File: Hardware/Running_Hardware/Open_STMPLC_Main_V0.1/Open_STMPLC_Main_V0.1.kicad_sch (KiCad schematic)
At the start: 44 parts, among them J1 Screw_Terminal_01x02, J2 Simcard_Nano, J4 DE9_Pins, J5 TF-102, Q1 Q_PMOS, U1 LAN8720A, U4 ADM2587E, U5 W25Q64JVSSIQ, U6 TPD4E1U06DCKR, U7 TPS26600PWP, U8 UCC23513

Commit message: schematic updates v0.1
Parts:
- removed C11: 33pF, Capacitor_SMD:C_0603_1608Metric_Pad1.08x0.95mm_HandSolder, symbol Device:C_Small
- removed D2: ESDA5V3SC5, Package_TO_SOT_SMD:SOT-23-5, symbol Power_Protection:ESDA5V3SC5
- removed D4: SS34, symbol Device:D_Schottky_Small
- removed J2: Simcard_Nano, SimCard:TE_2336582-1, symbol Simcard_Holder_Nano:47553-2001
- removed Q1: Q_PMOS, symbol Device:Q_PMOS
- added D2, D6, D7: SS54, symbol Device:D_Schottky_Small
- added D4: BZT52C12, symbol Device:D_Zener_Small
- added D5: SMAJ33CA, Diode_SMD:D_SMA, symbol Diode:SMAJ33CA
- added J2: Screw_Terminal_01x02, symbol Connector:Screw_Terminal_01x02
- added Q1: SUD50P06, Package_TO_SOT_SMD:TO-252-3_TabPin2, symbol Transistor_FET:Q_PMOS_GDS
- added Q2: AO3400A, Package_TO_SOT_SMD:SOT-23, symbol Transistor_FET:AO3400A
- added R10: 1K, symbol Device:R_Small
- added R11: 470R, symbol Device:R_Small
- added R12, R13: 150R, Resistor_SMD:R_0603_1608Metric_Pad0.98x0.95mm_HandSolder, symbol Device:R_Small
- added R14: 10K, symbol Device:R_Small
- added R15: 100K, symbol Device:R_Small
- added R16, R27, R3: 10K, Resistor_SMD:R_0603_1608Metric_Pad0.98x0.95mm_HandSolder, symbol Device:R_Small
- added R17, R19, R20: 4.7K, Resistor_SMD:R_0603_1608Metric_Pad0.98x0.95mm_HandSolder, symbol Device:R_Small
- added R18: 15K, symbol Device:R_Small
- added R4: 1K, Resistor_SMD:R_0603_1608Metric_Pad0.98x0.95mm_HandSolder, symbol Device:R_Small
- added R5: 715K, Resistor_SMD:R_0603_1608Metric_Pad0.98x0.95mm_HandSolder, symbol Device:R_Small
- added R8: 11.8K, Resistor_SMD:R_0603_1608Metric_Pad0.98x0.95mm_HandSolder, symbol Device:R_Small
- added R9: 33.2K, Resistor_SMD:R_0603_1608Metric_Pad0.98x0.95mm_HandSolder, symbol Device:R_Small
- added U10: MAX31865xTP, Package_DFN_QFN:TQFN-20-1EP_5x5mm_P0.65mm_EP3.25x3.25mm, symbol Sensor_Temperature:MAX31865xTP
- added U11: MAX31856, Package_SO:TSSOP-14_4.4x5mm_P0.65mm, symbol Sensor_Temperature:MAX31856
- added U12: 6N137, Package_DIP:DIP-8_W7.62mm, symbol Isolator:6N137
- added U3: TPS1H200A, Package_SO:HVSSOP-8-1EP_3x3mm_P0.65mm_EP1.57x1.89mm_ThermalVias, symbol TPS1H200A:TPS1H200A
- added U9: TPS3430WDRC, Package_SON:VSON-10-1EP_3x3mm_P0.5mm_EP1.65x2.4mm, symbol Power_Supervisor:TPS3430WDRC
- C10: value 33pF -> 620nF; footprint Capacitor_SMD:C_0603_1608Metric_Pad1.08x0.95mm_HandSolder -> (none); JLCPCB_Part C107047 -> (none)
- C8: value 100nF -> 1uF; footprint Capacitor_SMD:C_0402_1005Metric_Pad0.74x0.62mm_HandSolder -> (none); JLCPCB_Part C77020 -> (none)
- C9: value 33pF -> 2.2uF; footprint Capacitor_SMD:C_0603_1608Metric_Pad1.08x0.95mm_HandSolder -> (none); JLCPCB_Part C107047 -> (none)
- D1: value SS34 -> SS54
- R2: value 10K -> 47R
- R6: value 10K -> 20K; JLCPCB_Part C25804 -> (none)
- R7: value 51K -> 30.1K; JLCPCB_Part C23196 -> (none)
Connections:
- net USIM_CLK is gone; now on net GND: C10.2
- net USIM_DATA is gone; now on an unnamed net: R6.1
- net USIM_DET is gone; now on an unnamed net: R7.1
- net USIM_RST is gone; now on an unnamed net: C9.2
- net +24V: now also C8.1, D2.1 (K), D7.2 (A), R5.2
- net +3V3: now also R16.2, R27.2, R3.2, U12.8 (VCC); no longer R7.2
- net GND: now also C8.2, U1.25 (VSS), D5.2 (A2), J2.2 (Pin_2), Q2.2 (S), R10.1, R14.1, U10.10 (GND), U10.16 (GND), U10.21 (GND), U11.14 (DGND), U12.5 (GND), U3.6 (GND), U3.9 (EP), U9.11 (GND), U9.5 (GND); no longer C10.1, C8.1, C9.1
- net at D1.1 (K), D3.1 (A1), J1.1 (Pin_1): now also D2.2 (A)
- net at C1.1, C2.1, R2.2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: now also D4.1 (K), Q1.3 (S)
- net at D1.2 (A): now also Q1.2 (D)
- net at R1.2, R2.1: now also D4.2 (A), Q1.1 (G)
- net IMON: now reaches U7.10 (IMON)
- net IMON: now also R9.2
- net at U7.11 (ILIM): now also R8.2
- net at U7.12 (dVdT): now also C9.1
- net at U7.14 (~{FLT}): now also R3.1, R4.2
- net at U7.17 (RTN), U7.8 (RTN): now also U7.6 (MODE), R8.1, R9.1
- net at U7.3 (UVLO): now also R6.2, R5.1
- net at U7.5 (OVP): now also R7.2
- net ~{SHDN}: now reaches U7.7 (~{SHDN})
- net at U8.1 (ANODE): now also R12.2
- net at U8.3 (CATHODE): now also R13.2
- removed net USIM_VDD: C8.2, R6.2
- new net: Q2.3 (D), R13.1
- new net: Q2.1 (G), R11.2, R14.2
- new net: R10.2, U3.4 (CL)
- new net: C10.1, R15.1, U3.5 (DELAY)
- new net: D7.1 (K), R15.2, R18.2, U3.8 (VS)
- new net: D5.1 (A1), D6.1 (K), J2.1 (Pin_1)
- new net: D6.2 (A), R18.1, U3.7 (OUT)
- new net: R16.1, R17.2, U3.3 (~{FAULT})
- new net: R19.2, U3.1 (IN)
- new net: R20.2, U3.2 (DIAG_EN)
- new net +5V: R12.1
- new net DIAG_OUT1: R20.1
- new net HS_OUT_1: R11.1
- new net IN_1: R27.1, U12.6 (VO)
- new net LS_OUT1: R19.1
- new net ~{FAULT}: R17.1, R4.1
- no-connect marks 6 -> 8
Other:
- note removed: "Sim card"
- moved on the sheet: C1, C2, D1, D3, J1, R1, R2, U7, U8

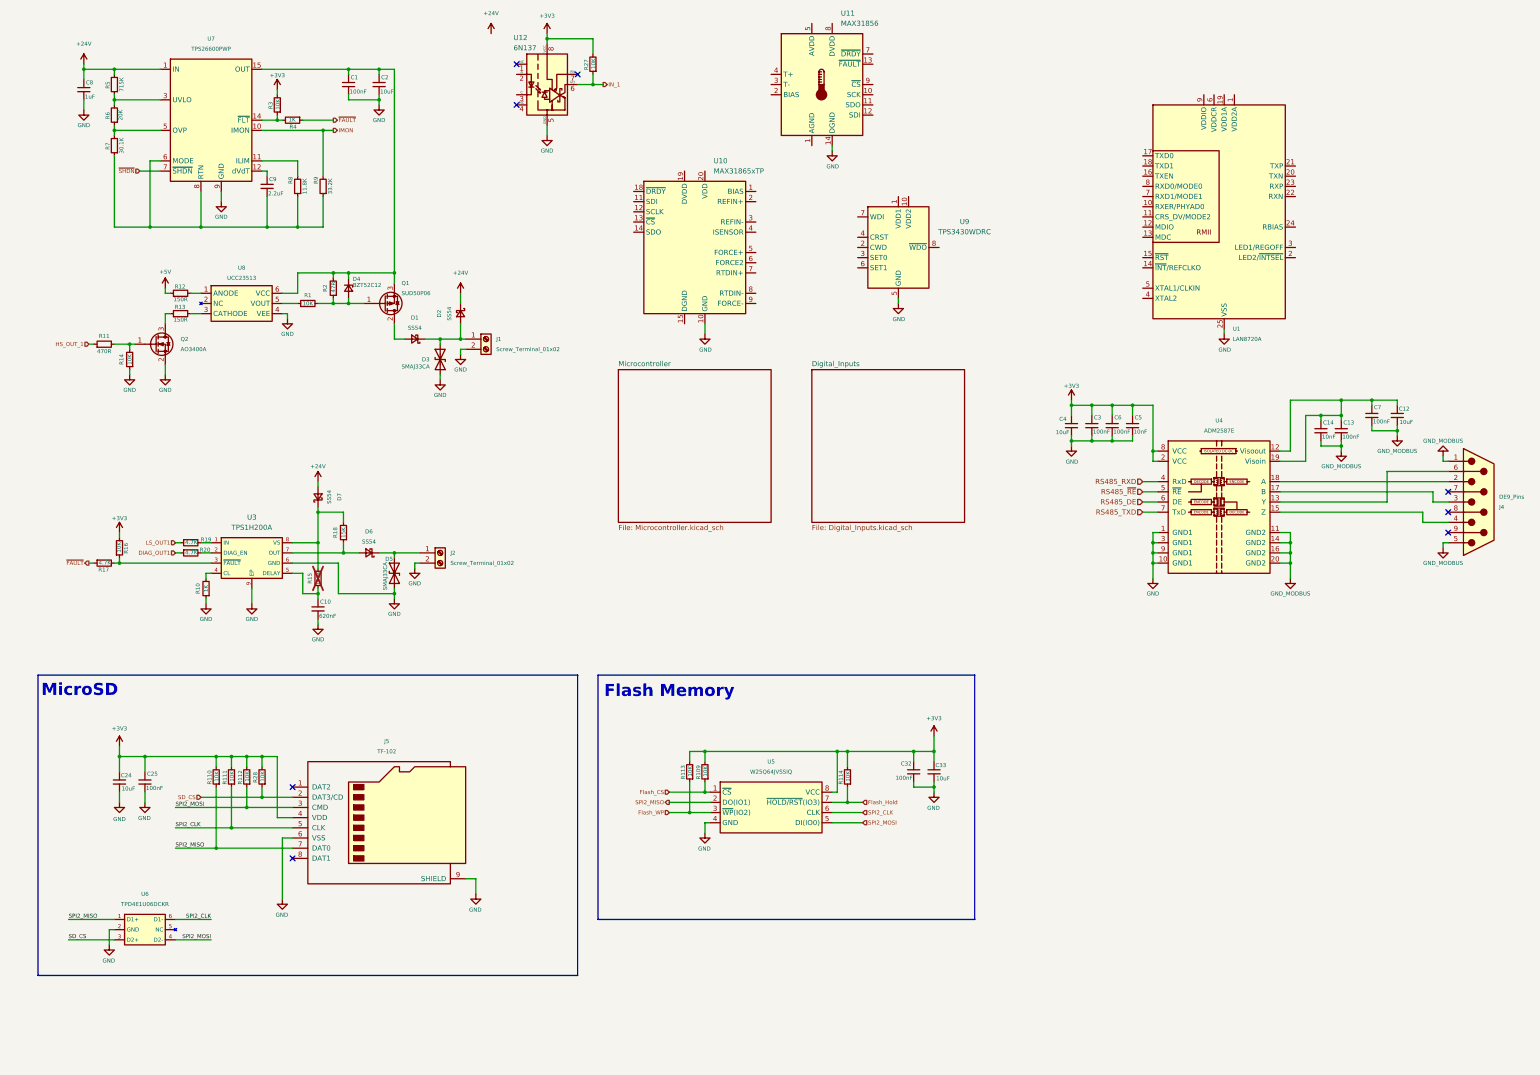
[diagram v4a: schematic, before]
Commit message: IO board schematic
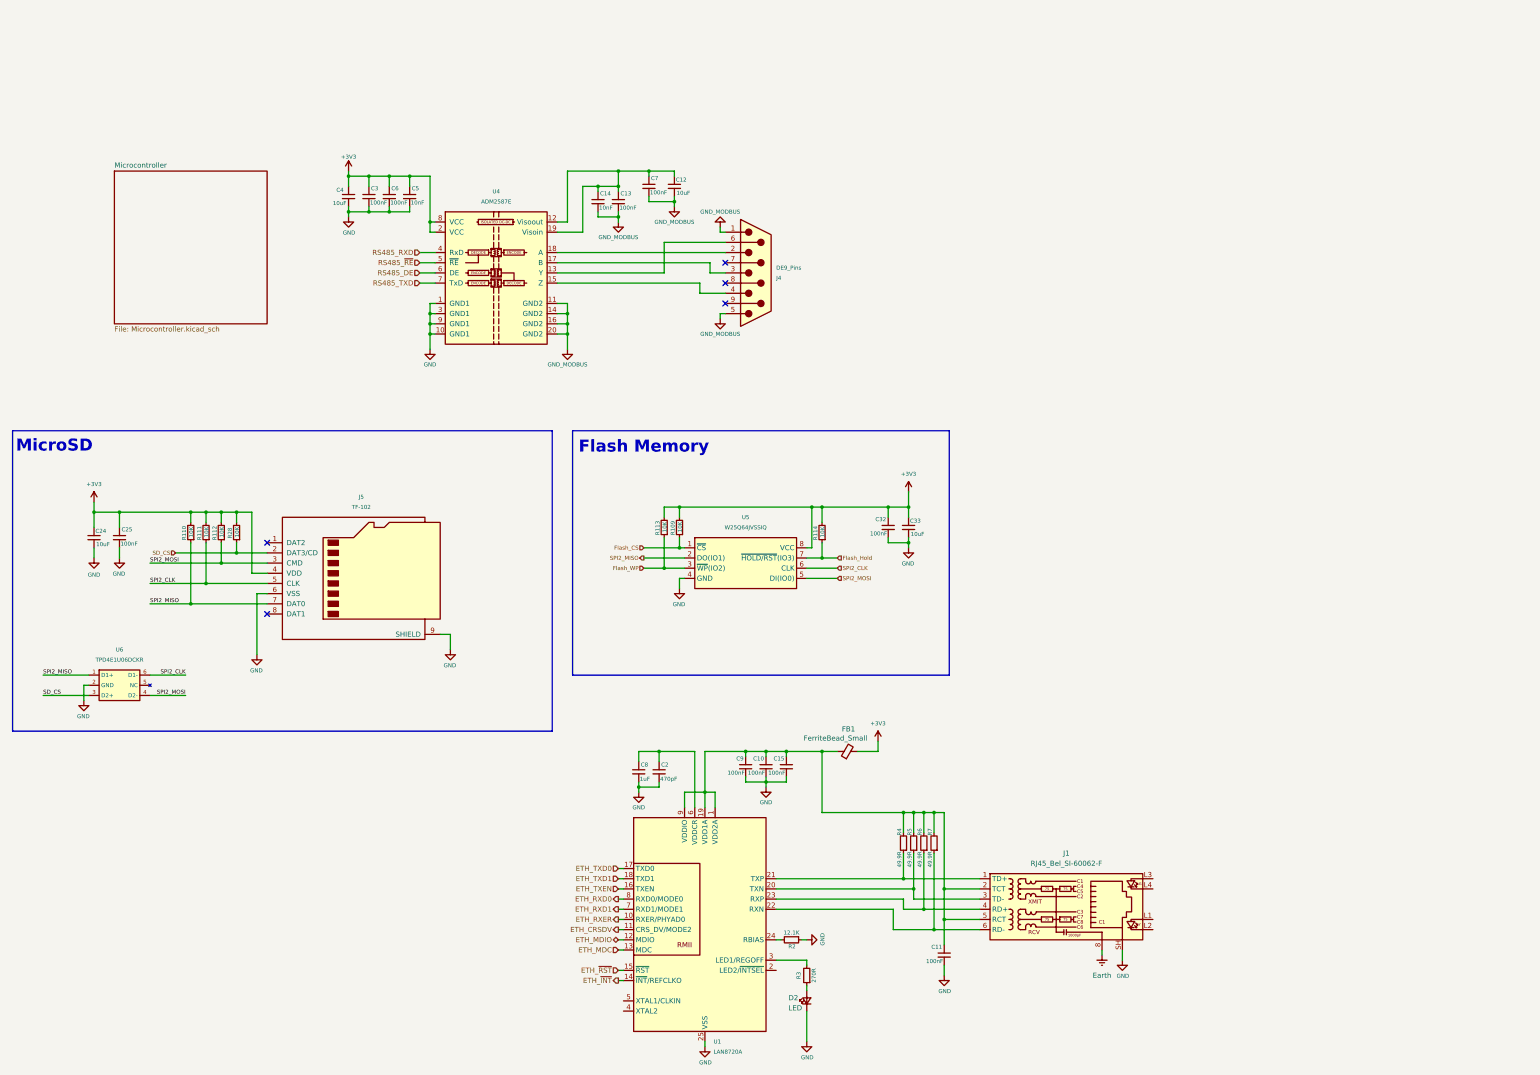
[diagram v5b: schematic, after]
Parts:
- removed C1: 100nF, symbol Device:C_Small
- removed D1, D2, D6, D7: SS54, symbol Device:D_Schottky_Small
- removed D3, D5: SMAJ33CA, Diode_SMD:D_SMA, symbol Diode:SMAJ33CA
- removed D4: BZT52C12, symbol Device:D_Zener_Small
- removed J1, J2: Screw_Terminal_01x02, symbol Connector:Screw_Terminal_01x02
- removed Q1: SUD50P06, Package_TO_SOT_SMD:TO-252-3_TabPin2, symbol Transistor_FET:Q_PMOS_GDS
- removed Q2: AO3400A, Package_TO_SOT_SMD:SOT-23, symbol Transistor_FET:AO3400A
- removed R1, R14: 10K, symbol Device:R_Small
- removed R10: 1K, symbol Device:R_Small
- removed R11: 470R, symbol Device:R_Small
- removed R12, R13: 150R, Resistor_SMD:R_0603_1608Metric_Pad0.98x0.95mm_HandSolder, symbol Device:R_Small
- removed R15: 100K, symbol Device:R_Small
- removed R16, R27: 10K, Resistor_SMD:R_0603_1608Metric_Pad0.98x0.95mm_HandSolder, symbol Device:R_Small
- removed R17, R19, R20: 4.7K, Resistor_SMD:R_0603_1608Metric_Pad0.98x0.95mm_HandSolder, symbol Device:R_Small
- removed R18: 15K, symbol Device:R_Small
- removed R8: 11.8K, Resistor_SMD:R_0603_1608Metric_Pad0.98x0.95mm_HandSolder, symbol Device:R_Small
- removed R9: 33.2K, Resistor_SMD:R_0603_1608Metric_Pad0.98x0.95mm_HandSolder, symbol Device:R_Small
- removed U10: MAX31865xTP, Package_DFN_QFN:TQFN-20-1EP_5x5mm_P0.65mm_EP3.25x3.25mm, symbol Sensor_Temperature:MAX31865xTP
- removed U11: MAX31856, Package_SO:TSSOP-14_4.4x5mm_P0.65mm, symbol Sensor_Temperature:MAX31856
- removed U12: 6N137, Package_DIP:DIP-8_W7.62mm, symbol Isolator:6N137
- removed U3: TPS1H200A, Package_SO:HVSSOP-8-1EP_3x3mm_P0.65mm_EP1.57x1.89mm_ThermalVias, symbol TPS1H200A:TPS1H200A
- removed U7: TPS26600PWP, Package_SO:HTSSOP-16-1EP_4.4x5mm_P0.65mm_EP3.4x5mm_Mask2.66x2.46mm_ThermalVias, symbol Power_Management:TPS26600PWP
- removed U8: UCC23513, Package_SO:SSO-6_6.8x4.6mm_P1.27mm_Clearance8mm, symbol UCC23153:UCC23513
- removed U9: TPS3430WDRC, Package_SON:VSON-10-1EP_3x3mm_P0.5mm_EP1.65x2.4mm, symbol Power_Supervisor:TPS3430WDRC
- added C11, C15: 100nF, Capacitor_SMD:C_0603_1608Metric_Pad1.08x0.95mm_HandSolder, symbol Device:C_Small
- added D2: LED, symbol Device:LED_Small
- added FB1: FerriteBead_Small, symbol Device:FerriteBead_Small
- added J1: RJ45_Bel_SI-60062-F, Connector_RJ:RJ45_Bel_SI-60062-F, symbol Connector:RJ45_Bel_SI-60062-F
- C10: value 620nF -> 100nF; footprint (none) -> Capacitor_SMD:C_0603_1608Metric_Pad1.08x0.95mm_HandSolder
- C2: value 10uF -> 470pF
- C9: value 2.2uF -> 100nF; footprint (none) -> Capacitor_SMD:C_0603_1608Metric_Pad1.08x0.95mm_HandSolder
- R2: value 47R -> 12.1K; footprint (none) -> Resistor_SMD:R_0603_1608Metric_Pad0.98x0.95mm_HandSolder
- R3: value 10K -> 270R; footprint Resistor_SMD:R_0603_1608Metric_Pad0.98x0.95mm_HandSolder -> (none)
- R4: value 1K -> 49.9R
- R5: value 715K -> 49.9R
- R6: value 20K -> 49.9R
- R7: value 30.1K -> 49.9R
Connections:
- net ~{FAULT} is gone; now on an unnamed net: R4.1
- net +3V3: now also FB1.2; no longer R3.2
- net GND: now also C9.2, R2.1, C11.2, C15.2, D2.1 (K), J1.SH
- net at R3.1: now also D2.2 (A); no longer R4.2
- net at R7.1: now also U1.22 (RXN), J1.6 (RD-); no longer C9.2
- net at R7.2: now also C10.1, C9.1, R4.2, R5.2, R6.2, U1.1 (VDD2A), U1.19 (VDD1A), U1.9 (VDDIO), C11.1, C15.1, FB1.1, J1.2 (TCT), J1.5 (RCT); no longer R6.1
- net at C2.1: now also C8.1, U1.6 (VDDCR); no longer R2.2
- net at R5.1: now also U1.20 (TXN), J1.3 (TD-); no longer R6.2
- net ETH_RXER: now reaches U1.10 (RXER/PHYAD0)
- net ETH_CRSDV: now reaches U1.11 (CRS_DV/MODE2)
- net ETH_MDIO: now reaches U1.12 (MDIO)
- net ETH_MDC: now reaches U1.13 (MDC)
- net ETH_~{INT}: now reaches U1.14 (~{INT}/REFCLKO)
- net ETH_~{RST}: now reaches U1.15 (~{RST})
- net ETH_TXEN: now reaches U1.16 (TXEN)
- net ETH_TXD0: now reaches U1.17 (TXD0)
- net ETH_TXD1: now reaches U1.18 (TXD1)
- net at U1.21 (TXP): now also J1.1 (TD+)
- net at U1.23 (RXP): now also R6.1, J1.4 (RD+)
- net at U1.24 (RBIAS): now also R2.2
- net at U1.3 (LED1/REGOFF): now also R3.2
- net ETH_RXD1: now reaches U1.7 (RXD1/MODE1)
- net ETH_RXD0: now reaches U1.8 (RXD0/MODE0)
- removed net +24V: C8.1, R5.2
- new net Earth: J1.8
- no-connect marks 8 -> 5
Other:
- removed sheet Digital_Inputs
- moved on the sheet: C12, C13, C14, C24, C25, C3, C32, C33, C4, C5, C6, C7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
